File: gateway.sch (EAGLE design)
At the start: 72 parts, among them J1 RASPBERRYPI-40-PIN-GPIO_PTH_N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, Q1 BSS123

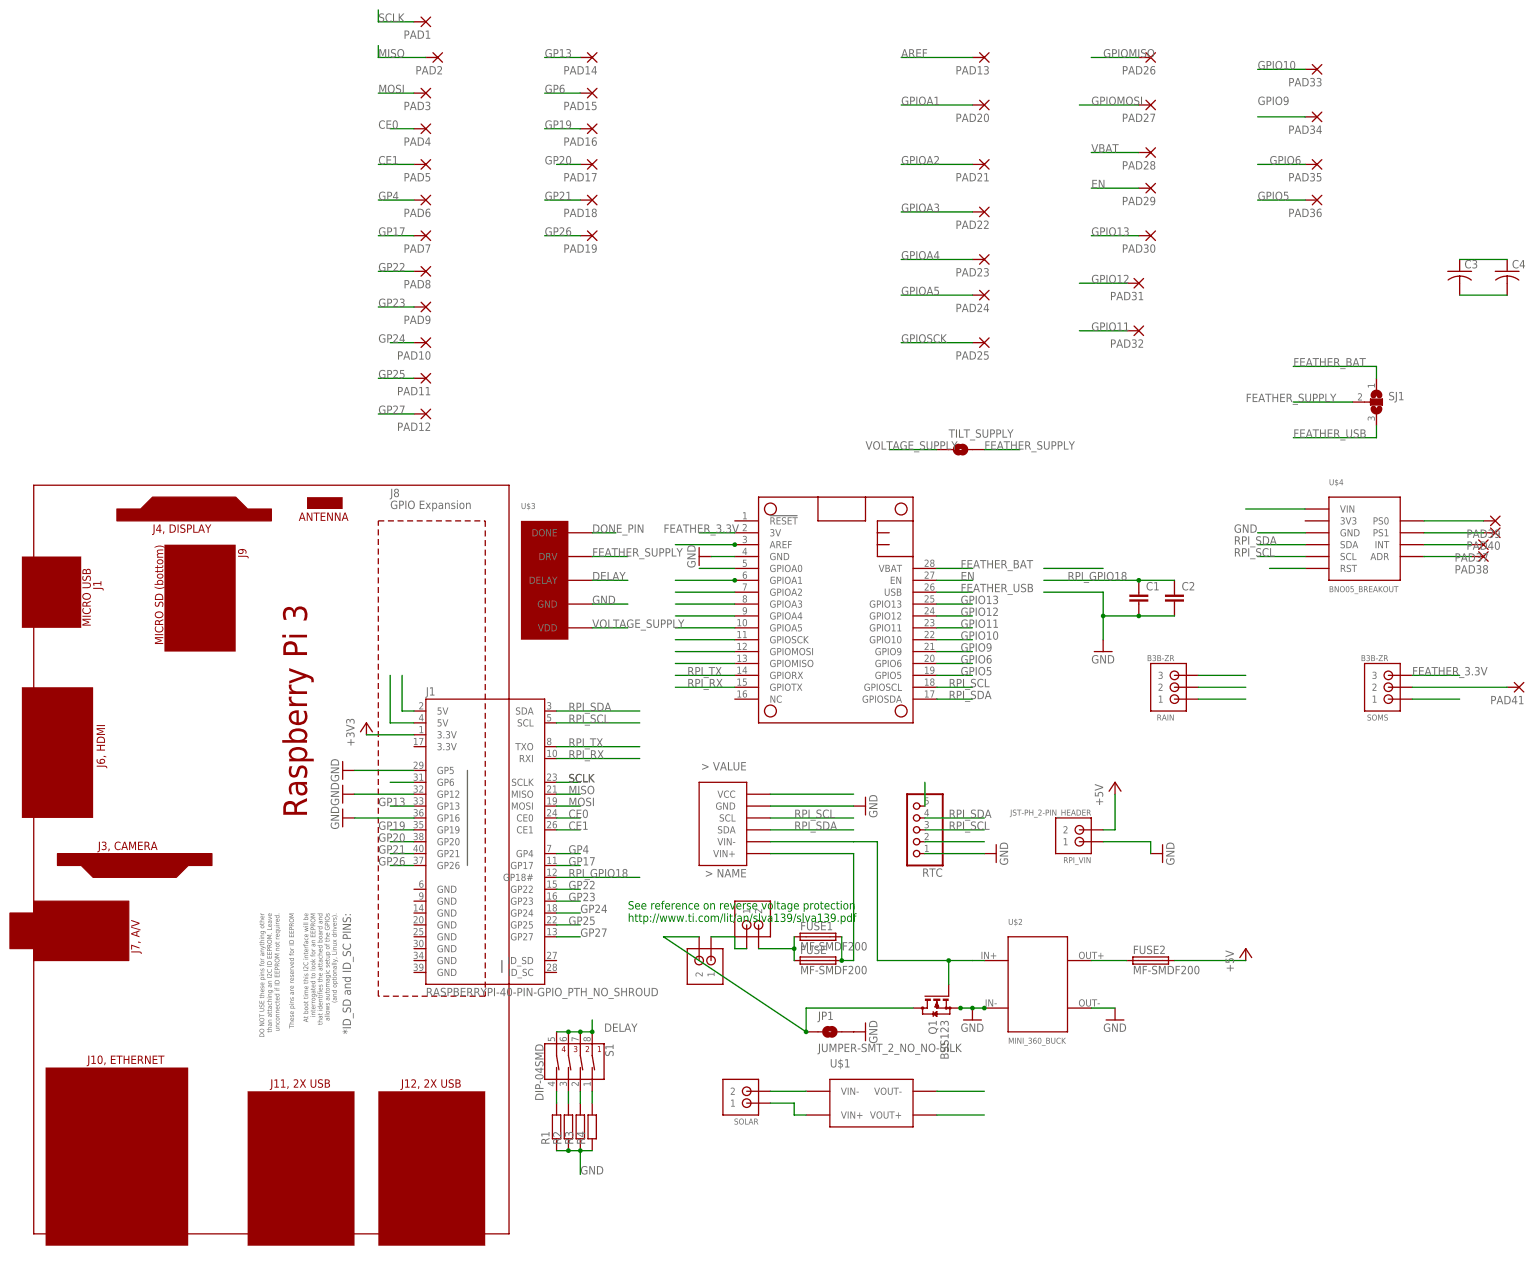
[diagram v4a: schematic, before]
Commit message: edc modules - larger pad size for dcdc gateway - right package for capacitor and fuse tilt board - no more timer module, embedded design, right packages for caps and fuse
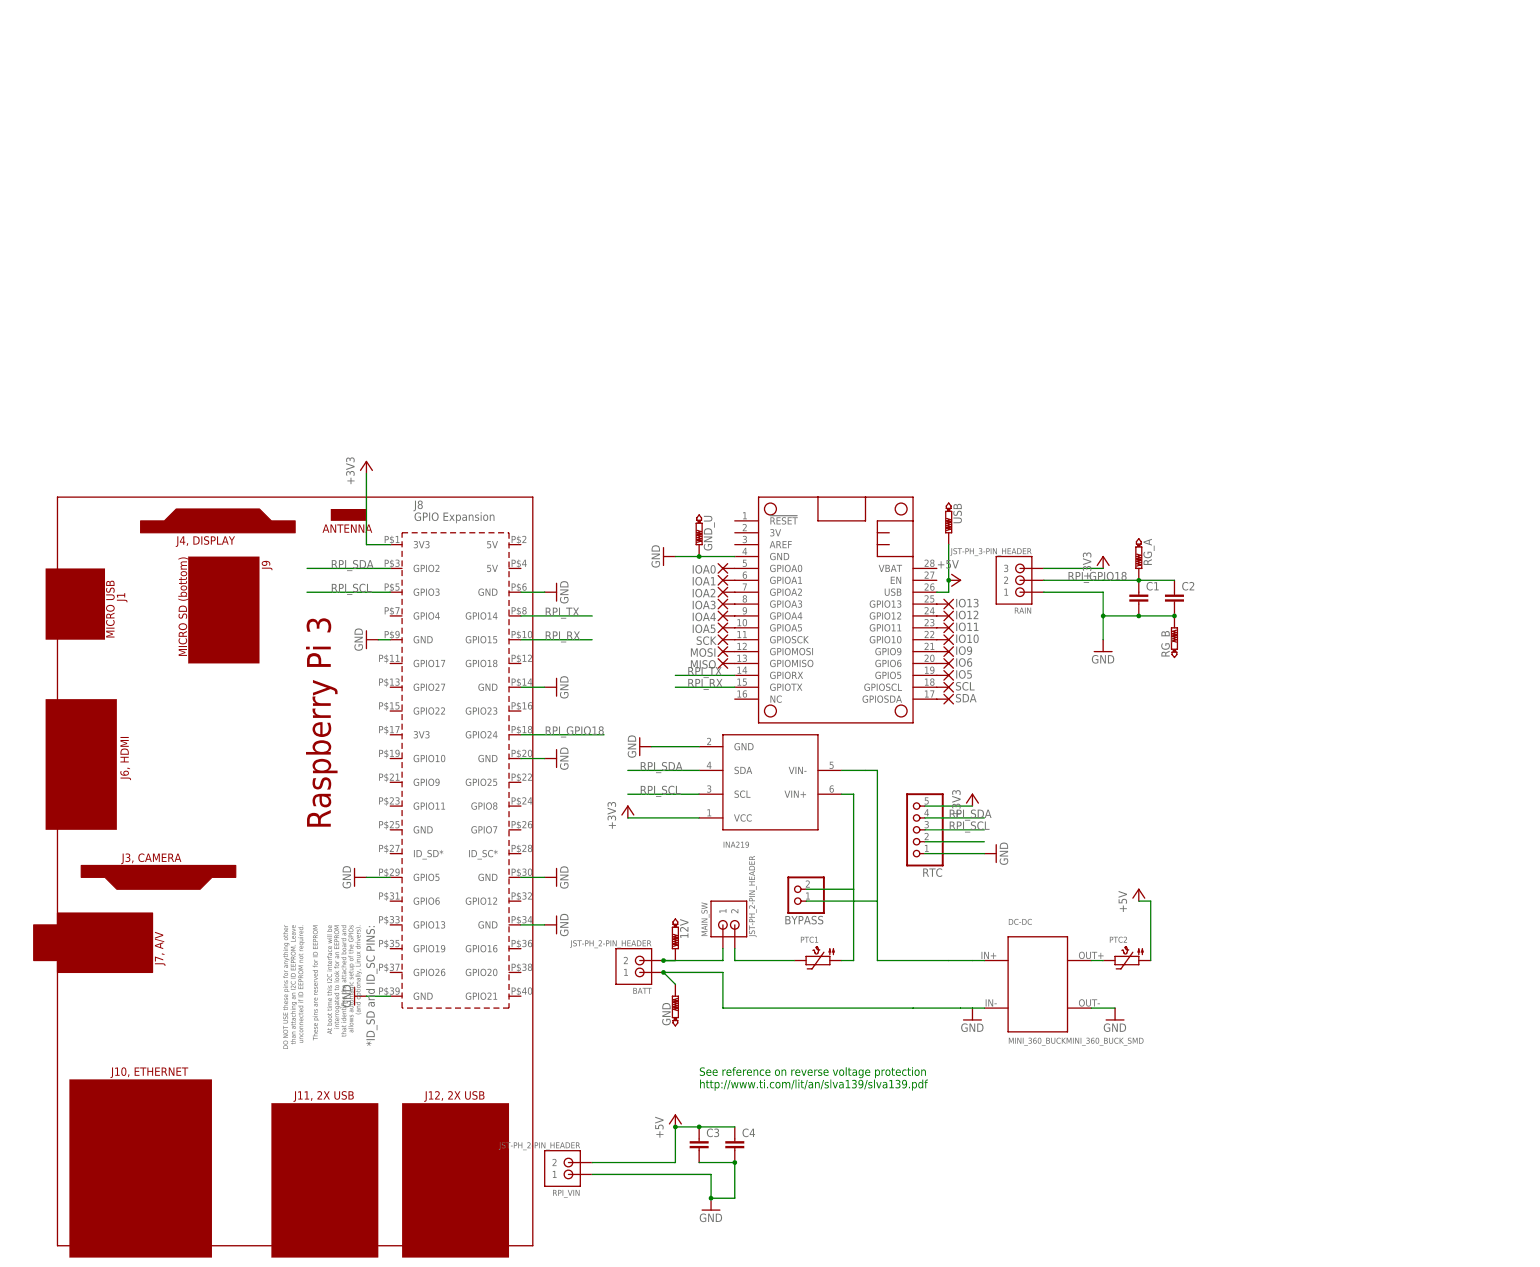
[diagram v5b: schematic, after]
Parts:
- removed FUSE, FUSE1, FUSE2: MF-SMDF200, fuse:MF-SMDF200
- removed J1: RASPBERRYPI-40-PIN-GPIO_PTH_NO_SHROUD, SparkFun-Connectors:RASPBERRYPI-40-PIN-GPIO_PTH_NO_SHROUD
- removed JP1, TILT_SUPPLY: JUMPER-SMT_2_NO_NO-SILK, SparkFun-Jumpers:JUMPER-SMT_2_NO_NO-SILK
- removed MAIN_SWITCH, SOLAR: JST-PH_2-PIN_HEADER, SRG:JST-PH_2-PIN_HEADER
- removed MS1: FEATHERWING_NODIM, adafruit:FEATHERWING_NODIM
- removed PAD1, PAD10, PAD11, PAD12, PAD13, PAD14, PAD15, PAD16, PAD17, PAD18, PAD19, PAD2, PAD20, PAD21, PAD22, PAD23, PAD24, PAD25, PAD26, PAD27, PAD28, PAD29, PAD3, PAD30, PAD31, PAD32, PAD33, PAD34, PAD35, PAD36, PAD37, PAD38, PAD39, PAD4, PAD40, PAD41, PAD5, PAD6, PAD7, PAD8, PAD9: WIREPADSMD1,27-254, wirepad:WIREPADSMD1,27-254
- removed Q1: BSS123, transistor-small-signal:BSS123
- removed R1, R2, R3, R4: (no value), rcl:R-EU_0204/5
- removed S1: DIP-04SMD, SparkFun-Switches:DIP-04SMD
- removed SJ1: (no value), jumper:SJ2W
- removed SOMS: B3B-ZR, jst:B3B-ZR
- removed U$1: TP5100, edc_modules:TP5100
- removed U$2: MINI_360_BUCK, edc_modules:MINI_360_BUCK
- removed U$3: TPL5110_BREAKOUT, edc_modules:TPL5110_BREAKOUT
- removed U$4: BNO05_BREAKOUT, edc_modules:BNO05_BREAKOUT
- added 12V, GND, GND_U, RG_A, RG_B, USB: PTR1PAD1-13, testpad:PTR1PAD1-13
- added BYPASS: (no value), pinhead:PINHD-1X2
- added DC-DC: MINI_360_BUCKMINI_360_BUCK_SMD, edc_modules:MINI_360_BUCKMINI_360_BUCK_SMD
- added IO10, IO11, IO12, IO13, IO5, IO6, IO9, IOA0, IOA1, IOA2, IOA3, IOA4, IOA5, MISO, MOSI, SCK, SCL, SDA: (no value), wirepad:SMD2
- added MAIN_SW: JST-PH_2-PIN_HEADER, SRG:JST-PH_2-PIN_HEADER
- added MS2: FEATHERWINGFEATHERWING_EDC, adafruit:FEATHERWINGFEATHERWING_EDC
- added PTC1: (no value), microbuilder:PTC1206
- added PTC2: (no value), microbuilder:PTC1210
- C3: device rcl:C-USC1812 -> rcl:C-EUC1210
- C4: device rcl:C-USC1812 -> rcl:C-EUC2012
- PCB2: value RPI3_NO_GPIO -> RPI3; device e14_Rpi3_RevA:RPI3_NO_GPIO -> e14_Rpi3_RevA:RPI3
- RAIN: value B3B-ZR -> JST-PH_3-PIN_HEADER; device jst:B3B-ZR -> SRG:JST-PH_3-PIN_HEADER
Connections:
- removed net AREF: MS1.AREF, PAD13.P
- removed net BATT+: FUSE.1, FUSE1.1, MAIN_SWITCH.2, U$1.VOUT+
- removed net BATT-: BATT.2, JP1.1, Q1.D, U$1.VOUT-
- removed net CE0: J1.CE0, PAD4.P
- removed net CE1: J1.CE1, PAD5.P
- removed net DELAY: S1.1B, S1.2B, S1.3B, S1.4B, U$3.DELAY
- removed net DONE_PIN: MS1.GPIOA0, U$3.DONE
- removed net EN: MS1.EN, PAD29.P
- removed net FEATHER_3.3V: INA219.VCC, MS1.3V, RAIN.3, RTC.5, SOMS.3, U$4.VIN
- removed net FEATHER_BAT: MS1.VBAT, SJ1.1
- removed net FEATHER_SUPPLY: SJ1.2, TILT_SUPPLY.2, U$3.DRV
- removed net FEATHER_USB: MS1.USB, SJ1.3
- removed net GP13: J1.GP13, PAD14.P
- removed net GP17: J1.GP17, PAD7.P
- removed net GP19: J1.GP19, PAD16.P
- removed net GP20: J1.GP20, PAD17.P
- removed net GP21: J1.GP21, PAD18.P
- removed net GP22: J1.GP22, PAD8.P
- removed net GP23: J1.GP23, PAD9.P
- removed net GP24: J1.GP24, PAD10.P
- removed net GP25: J1.GP25, PAD11.P
- removed net GP26: J1.GP26, PAD19.P
- removed net GP27: J1.GP27, PAD12.P
- removed net GP4: J1.GP4, PAD6.P
- removed net GP6: J1.GP6, PAD15.P
- removed net GPIO10: MS1.GPIO10, PAD33.P
- removed net GPIO11: MS1.GPIO11, PAD32.P
- removed net GPIO12: MS1.GPIO12, PAD31.P
- removed net GPIO13: MS1.GPIO13, PAD30.P
- removed net GPIO5: MS1.GPIO5, PAD36.P, U$4.RST
- removed net GPIO6: MS1.GPIO6, PAD35.P
- removed net GPIO9: MS1.GPIO9, PAD34.P
- removed net GPIOA1: MS1.GPIOA1, PAD20.P
- removed net GPIOA2: MS1.GPIOA2, PAD21.P
- removed net GPIOA3: MS1.GPIOA3, PAD22.P
- removed net GPIOA4: MS1.GPIOA4, PAD23.P
- removed net GPIOA5: MS1.GPIOA5, PAD24.P
- removed net GPIOMISO: MS1.GPIOMISO, PAD26.P
- removed net GPIOMOSI: MS1.GPIOMOSI, PAD27.P
- removed net GPIOSCK: MS1.GPIOSCK, PAD25.P
- removed net INA_VIN+: FUSE.2, FUSE1.2, INA219.VIN+
- removed net INA_VIN-: INA219.VIN-, Q1.G, U$2.VIN+
- removed net MISO: J1.MISO, PAD2.P
- removed net MOSI: J1.MOSI, PAD3.P
- removed net SCLK: J1.SCLK, PAD1.P
- removed net SOLAR+: SOLAR.1, U$1.VIN+
- removed net SOLAR-: SOLAR.2, U$1.VIN-
- removed net VBAT: PAD28.P
- removed net VOLTAGE_SUPPLY: C3.1, C4.1, FUSE2.2, RPI_VIN.2, TILT_SUPPLY.1, U$3.VDD
- new net +5V: C3.1, C4.1, MS2.USB, PTC2.1, RPI_VIN.2, USB.TP
- new net N$14: IO13.P, MS2.GPIO13
- new net N$16: MOSI.P, MS2.GPIOMOSI
- new net N$17: MS2.GPIOSCK, SCK.P
- new net N$18: IOA5.P, MS2.GPIOA5
- new net N$19: IOA4.P, MS2.GPIOA4
- new net N$20: IOA3.P, MS2.GPIOA3
- new net N$21: IOA2.P, MS2.GPIOA2
- new net N$22: IOA1.P, MS2.GPIOA1
- new net N$23: IOA0.P, MS2.GPIOA0
- new net N$24: DC-DC.VOUT+, PTC2.2
- net +3V3: now also INA219.VCC, PCB2.3V3@1, RAIN.3, RTC.5; no longer J1.3.3V@1
- net GND: now also BATT.1, DC-DC.VIN-, DC-DC.VOUT-, GND.TP, GND_U.TP, MS2.GND, PCB2.GND@14, PCB2.GND@20, PCB2.GND@30, PCB2.GND@34, PCB2.GND@39, PCB2.GND@6, PCB2.GND@9, PCB2.GPIO5, RG_B.TP; no longer J1.GP12, J1.GP16, J1.GP5, JP1.2, MS1.GND, Q1.S, R1.1, R2.1, R3.1, R4.1, SOMS.1, U$2.VIN-, U$2.VOUT-, U$3.GND, U$4.GND
- net N$1: now also MS2.GPIOSDA, SDA.P; no longer PAD37.P, U$4.INT
- net N$10: now also IO9.P, MS2.GPIO9; no longer R2.2, S1.3A
- net N$11: now also IO10.P, MS2.GPIO10; no longer R3.2, S1.2A
- net N$12: now also IO11.P, MS2.GPIO11; no longer R4.2, S1.1A
- net N$13: now also IO12.P, MS2.GPIO12; no longer BATT.1, MAIN_SWITCH.1
- net N$15: now also MISO.P, MS2.GPIOMISO; no longer PAD41.P, SOMS.2
- net N$2: now also 12V.TP, BATT.2, MAIN_SW.1; no longer J1.5V@2
- net N$3: now also MAIN_SW.2, PTC1.2; no longer J1.5V@4
- net N$5: now also BYPASS.1, DC-DC.VIN+, INA219.VIN-; no longer PAD38.P, U$4.ADR
- net N$6: now also BYPASS.2, INA219.VIN+, PTC1.1; no longer PAD39.P, U$4.PS0
- net N$7: now also MS2.GPIOSCL, SCL.P; no longer PAD40.P, U$4.PS1
- net N$8: now also IO5.P, MS2.GPIO5; no longer FUSE2.1, U$2.VOUT+
- net N$9: now also IO6.P, MS2.GPIO6; no longer R1.2, S1.4A
- net RPI_GPIO18: now also PCB2.GPIO24, RG_A.TP; no longer J1.GP18#
- net RPI_RX: now also MS2.GPIOTX, PCB2.GPIO15; no longer J1.RXI, MS1.GPIOTX
- net RPI_SCL: now also PCB2.GPIO3; no longer J1.SCL, MS1.GPIOSCL, U$4.SCL
- net RPI_SDA: now also PCB2.GPIO2; no longer J1.SDA, MS1.GPIOSDA, U$4.SDA
- net RPI_TX: now also MS2.GPIORX, PCB2.GPIO14; no longer J1.TXO, MS1.GPIORX
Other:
- moved on the sheet: C3, C4, RAIN, RPI_VIN
